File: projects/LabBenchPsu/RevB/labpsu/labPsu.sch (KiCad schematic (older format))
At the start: 45 parts

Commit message: working on schematic
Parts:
- removed C?: 100nF, symbol C
- removed R?: 1K, symbol R
- R2: renamed from R?; value 10K -> 18K
- gave numbers to parts that had none: 41
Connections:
- net 3V3_Reg: now also C2.1, U2.2 (VO), U2.4 (VO)
- net GND: now also C7.2, C8.2, R11.1, U6.~ (V-)
- no-connect marks 8 -> 21
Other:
- note added: "0-3.3V PWM IN\n0-2.12V DC OUT"
- note added: "Additional load resistors\nfan control (3pin?)\nOpamp : single supply operation"
- note added: "DAC"
- note added: "constant current \ndrain of 677uA"
- note added: "current drain \nof about 50uA"
- note removed: "Additional load resistors\nfan control (3pin?)"
- moved on the sheet: P4, P5, P6, P7, U4

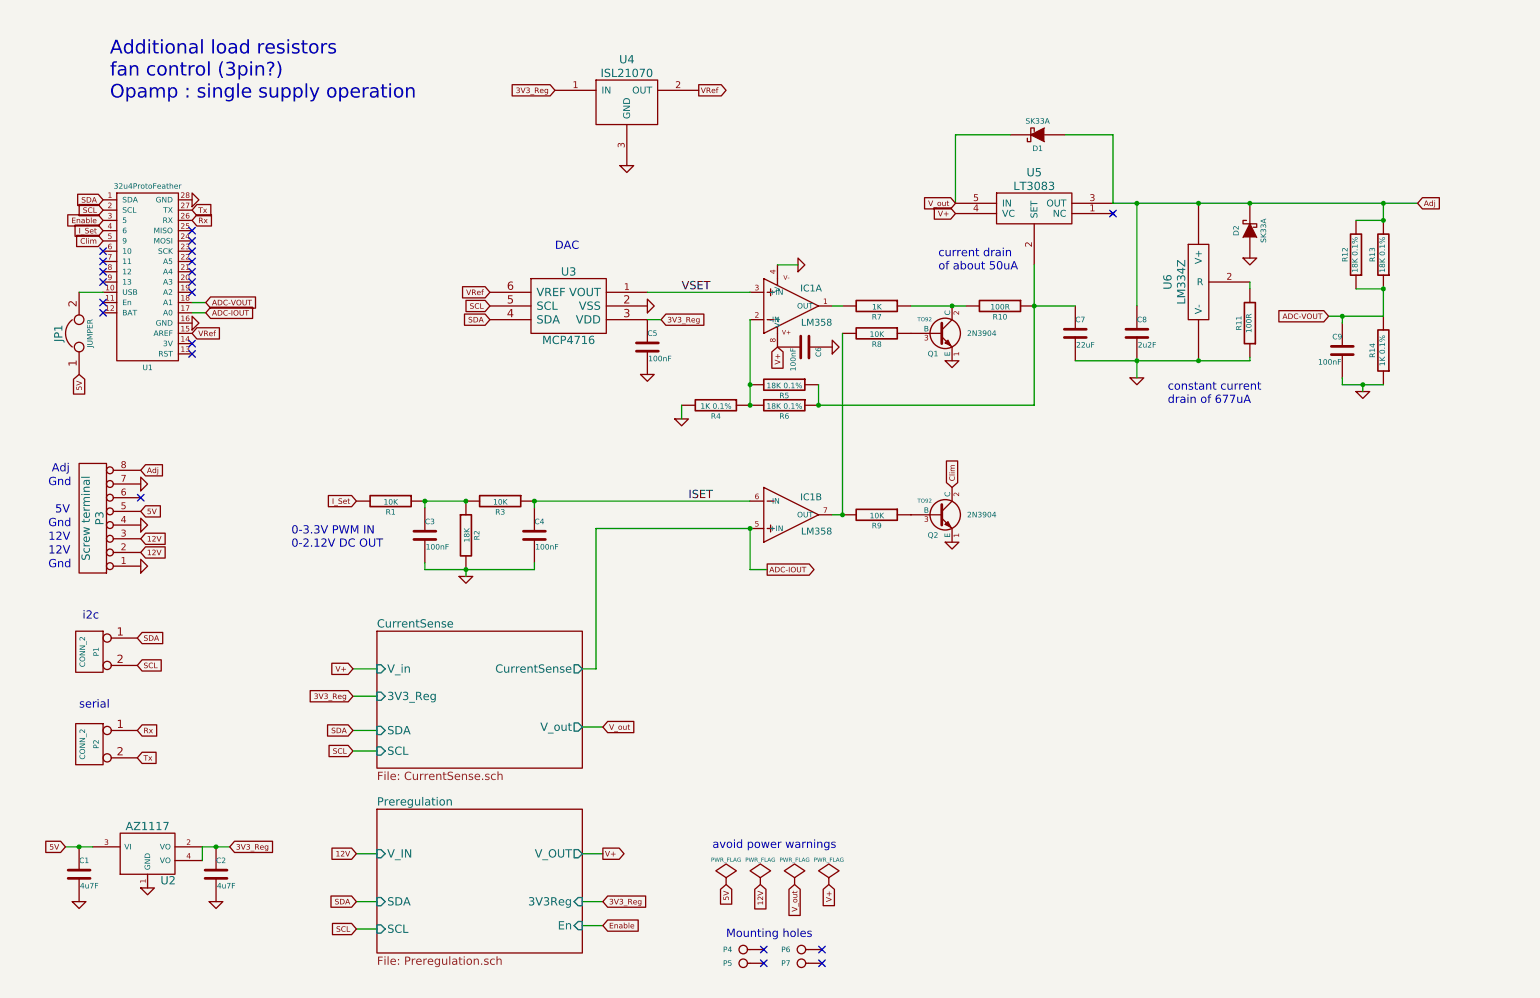
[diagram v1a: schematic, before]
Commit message: redraw schematic
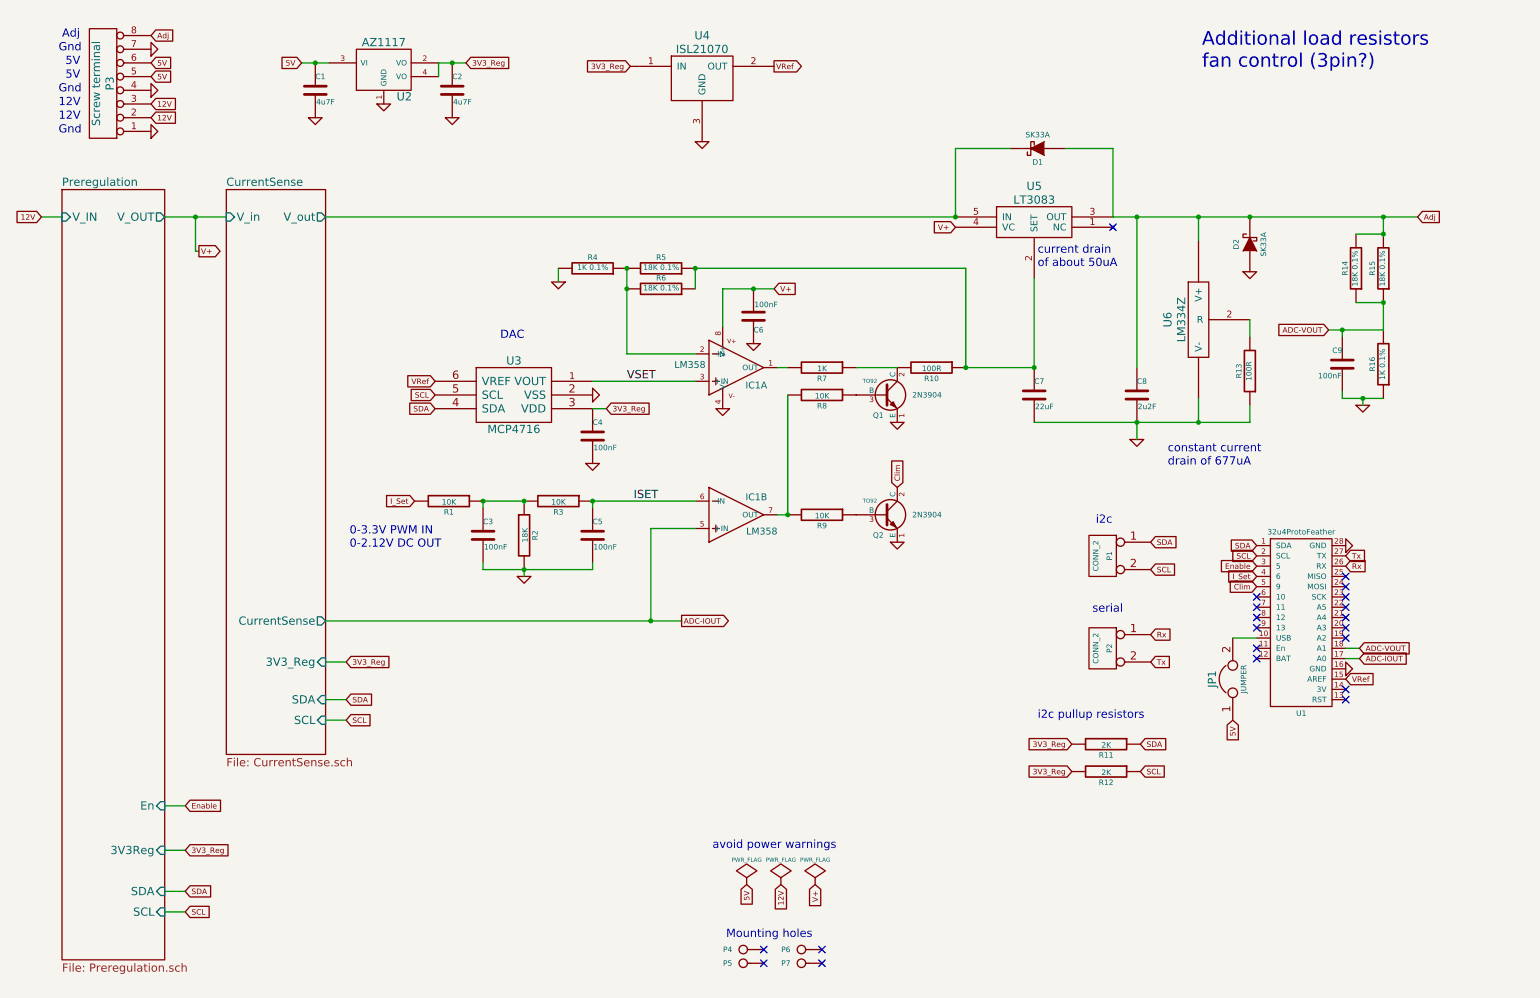
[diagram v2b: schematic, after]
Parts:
- added R11, R12: 2K, symbol R
- renumbered C5 to C4, C4 to C5, R11 to R13, R12 to R14, R13 to R15, R14 to R16, R6 to R5, R5 to R6
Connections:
- net 3V3_Reg: now also R11.2, R12.2
- net 5V: now also P3.6 (P6)
- net SCL: now also R12.1
- net SDA: now also R11.1
- net V_out renamed CurrentSense/V_out
- no-connect marks 21 -> 20
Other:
- note added: "Additional load resistors\nfan control (3pin?)"
- note added: "i2c pullup resistors"
- note removed: "Additional load resistors\nfan control (3pin?)\nOpamp : single supply operation"
- moved on the sheet: C1, C2, C3, C4, C5, C6, C7, C8, C9, D1, D2, IC1A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

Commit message: constant current load added
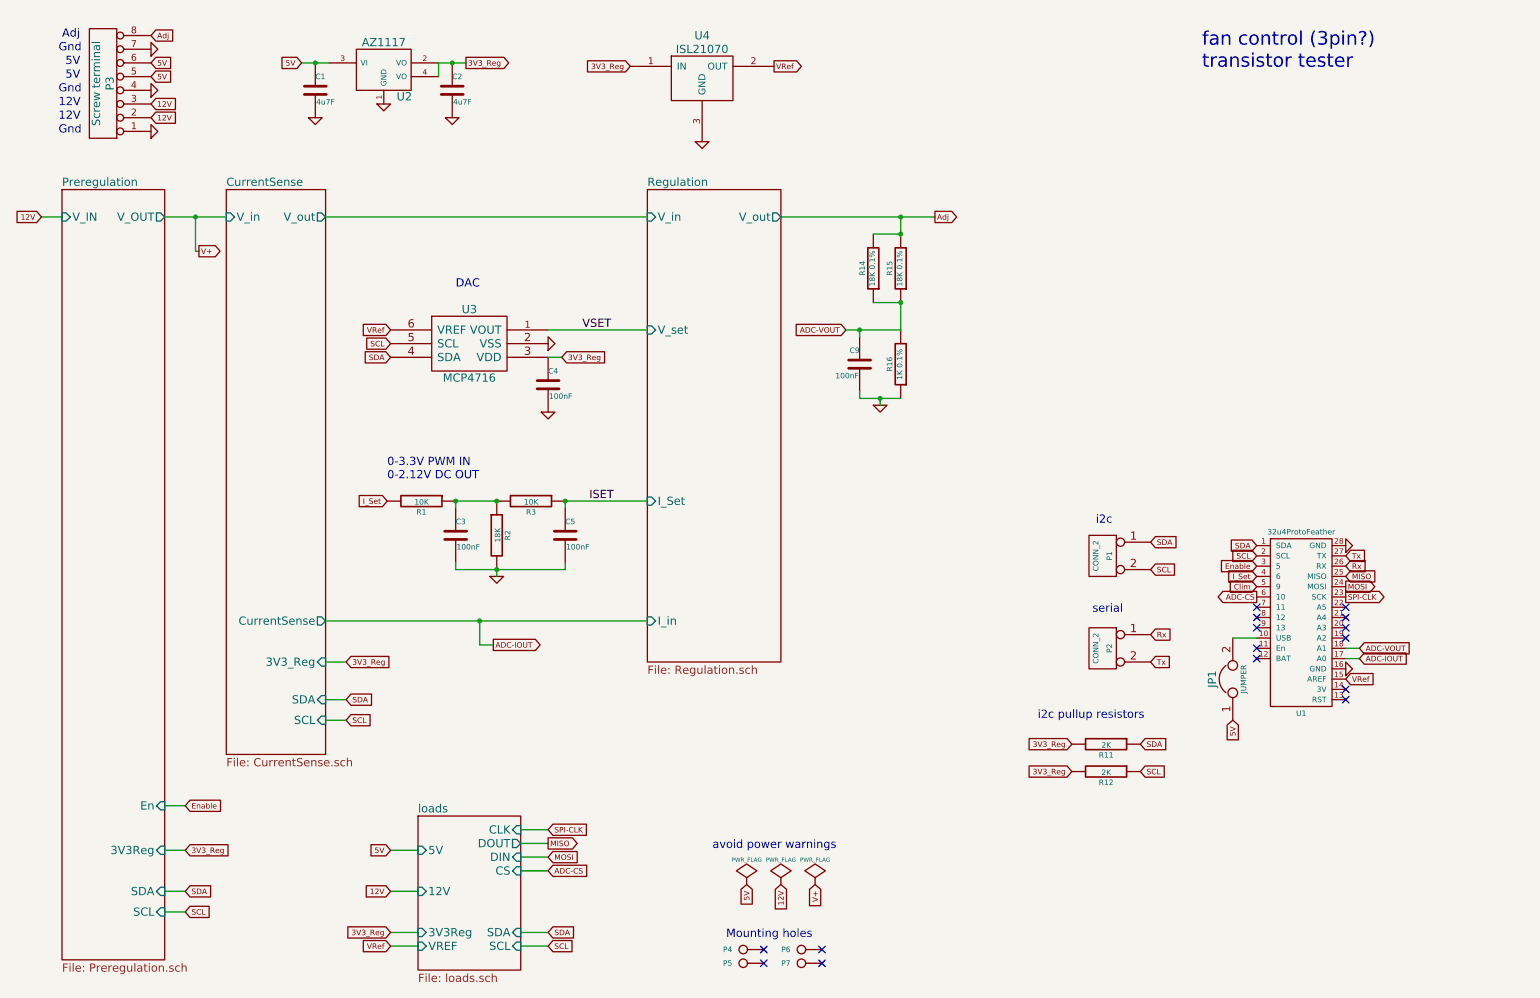
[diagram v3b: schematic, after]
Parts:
- removed C6: 100nF, symbol C
- removed C7: 22uF, symbol C
- removed C8: 2u2F, symbol C
- removed D1, D2: SK33A, symbol DIODESCH
- removed IC1: LM358, SparkFun-SO08, symbol OPAMP-DUALU
- removed Q1, Q2: 2N3904, TO92, symbol 2N3904
- removed R10, R13: 100R, symbol R
- removed R4: 1K 0.1%, symbol R
- removed R5, R6: 18K 0.1%, symbol R
- removed R7: 1K, symbol R
- removed R8, R9: 10K, symbol R
- removed U5: LT3083, symbol LT3083
- removed U6: LM334Z, symbol LM334Z
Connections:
- net SPI-CLK: now reaches U1.23 (SCK)
- net MOSI: now reaches U1.24 (MOSI)
- net MISO: now reaches U1.25 (MISO)
- net ADC-CS: now reaches U1.6 (10)
- no-connect marks 20 -> 15
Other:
- note added: "fan control (3pin?)\ntransistor tester"
- note removed: "Additional load resistors\nfan control (3pin?)"
- note removed: "constant current \ndrain of 677uA"
- note removed: "current drain \nof about 50uA"
- moved on the sheet: C3, C4, C5, C9, R1, R14, R15, R16, R2, R3, U3

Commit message: schematic more or less done
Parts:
- added C28, C29, C30: 100nF, symbol C
- added D4, D5: DIODE, symbol DIODE
- added IC5: LM324, symbol OPAMP-DUALU
- added K1, K2: CONN_3, symbol CONN_3
- added Q4, Q5: PN2222, symbol 2N3904
- added R56, R57, R58, R59, R60, R61: 10K, symbol R
- added R62, R63: 5K, symbol R
- renumbered C9 to C6, P3 to P1, P4 to P2, P5 to P3, P6 to P4, P7 to P5, P1 to P6, P2 to P7, R14 to R4, R15 to R5, R16 to R6, R11 to R7, R12 to R8, U2 to U1, U3 to U2, U4 to U3, U1 to U4
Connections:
- net 12V: now also D4.2 (K), D5.2 (K), K1.2 (PM), K2.2 (PM)
- net 3V3_Reg: now also R62.2, R63.2
- net 5V: now also C30.1, IC5.8 (V+)
- net GND: now also C28.2, C29.2, C30.2, IC5.4 (V-), Q4.1 (E), Q5.1 (E), R58.2, R59.2
- net I_load: now reaches U4.19 (A2)
- net V_load: now reaches U4.20 (A3)
- net sense1: now reaches U4.21 (A4)
- net sense1: now also K1.3 (P3), R62.1
- net sense2: now reaches U4.22 (A5)
- net sense2: now also K2.3 (P3), R63.1
- net fan2: now reaches U4.7 (11)
- net fan2: now also R57.2
- net ADC-CS renamed fan1
- net fan1: now also R56.2
- net MISO: no longer names the net of U4.25 (MISO)
- net MOSI: no longer names the net of U4.24 (MOSI)
- net SPI-CLK: no longer names the net of U4.23 (SCK)
- new net: IC5.1 (OUT), Q4.3 (B), R60.1
- new net: IC5.2 (-IN), R58.1, R60.2
- new net: C28.1, IC5.3 (+IN), R56.1
- new net: C29.1, IC5.5 (+IN), R57.1
- new net: IC5.6 (-IN), R59.1, R61.2
- new net: IC5.7 (OUT), Q5.3 (B), R61.1
- new net: D4.1 (A), K1.1 (P1), Q4.2 (C)
- new net: D5.1 (A), K2.1 (P1), Q5.2 (C)
- no-connect marks 15 -> 13
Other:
- note added: "0-2V VSET \n(for 0-20V Vout)"
- note added: "GND"
- note added: "SENSE"
- note added: "amplifier 2x\nbase signal = 2x fan-signal"
- note added: "fan control"
- note removed: "fan control (3pin?)\ntransistor tester"

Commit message: schematic reviewed
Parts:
- removed U2: MCP4716, symbol MCP4716
- added U2: MCP4725, symbol MCP4725
- IC5: value LM324 -> LM358
- R62, R63: value 5K -> 4K7
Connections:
- net 3V3_Reg: now also U2.3 (VDD), U2.6 (A0)
- net GND: now also U2.2 (VSS)
- net SCL: now also U2.5 (SCL)
- net SDA: now also U2.4 (SDA)
- net VSET: now also U2.1 (VOUT)
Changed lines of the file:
@@
-	1    0    0    -1
-$EndComp
-$Comp
-L MCP4716 U2
-U 1 1 57DE2995
-P 3825 3050
-F 0 "U2" H 3825 3300 60  0000 C CNN
-F 1 "MCP4716" H 3825 2800 60  0000 C CNN
-F 2 "" H 3825 2925 60  0001 C CNN
-F 3 "" H 3825 2925 60  0000 C CNN
-	1    3825 3050
 	1    0    0    -1
 $EndComp
@@
 Text GLabel 10225 5275 2    40   Input ~ 0
 ADC-VOUT
-Text GLabel 6575 2950 0    40   Input ~ 0
+Text GLabel 6575 2950 0    40   Output ~ 0
 ADC-VOUT
 Text GLabel 4000 5250 2    40   Output ~ 0
@@
 	0    -1   -1   0
 $EndComp
-Text GLabel 3250 2950 0    40   Input ~ 0
-VRef
 Text Notes 3225 4050 0    60   ~ 0
 0-3.3V PWM IN\n0-2.12V DC OUT
@@
 P 8575 1450
 F 0 "IC5" H 8850 1350 50  0000 R TNN
-F 1 "LM324" H 8950 1600 50  0000 R TNN
+F 1 "LM358" H 8950 1600 50  0000 R TNN
 F 2 "" H 8575 1600 50  0001 C CNN
 F 3 "" H 8575 1450 60  0000 C CNN
@@
 P 8675 2700
 F 0 "IC5" H 8850 2850 50  0000 R TNN
-F 1 "LM324" H 8950 2600 50  0000 R TNN
+F 1 "LM358" H 8950 2600 50  0000 R TNN
 F 2 "" H 8675 2850 50  0001 C CNN
 F 3 "" H 8675 2700 60  0000 C CNN
@@
 P 10450 3200
 F 0 "R63" V 10530 3200 40  0000 C CNN
-F 1 "5K" V 10457 3201 40  0000 C CNN
+F 1 "4K7" V 10457 3201 40  0000 C CNN
 F 2 "" V 10380 3200 30  0001 C CNN
 F 3 "" H 10450 3200 30  0000 C CNN
@@
 P 10450 1950
 F 0 "R62" V 10530 1950 40  0000 C CNN
-F 1 "5K" V 10457 1951 40  0000 C CNN
+F 1 "4K7" V 10457 1951 40  0000 C CNN
 F 2 "" V 10380 1950 30  0001 C CNN
 F 3 "" H 10450 1950 30  0000 C CNN
@@
 Text Notes 4300 2800 0    60   ~ 0
 0-2V VSET \n(for 0-20V Vout)
+$Comp
+L MCP4725 U2
+U 1 1 5818A13D
+P 3825 3050
+F 0 "U2" H 3825 3300 60  0000 C CNN
+F 1 "MCP4725" H 3825 2800 60  0000 C CNN
+F 2 "" H 3825 2925 60  0000 C CNN
+F 3 "" H 3825 2925 60  0000 C CNN
+	1    3825 3050
+	1    0    0    -1
+$EndComp
+Text GLabel 3250 2950 0    40   Input ~ 0
+3V3_Reg
 $EndSCHEMATC
